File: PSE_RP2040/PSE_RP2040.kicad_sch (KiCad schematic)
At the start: 57 parts, among them IC1 AT25SF128A-SHB-T, IC2 SAM-M8Q-0, J1 USB_B, J2 USB_B_Micro, J3 Conn_01x02, U1 RP2040

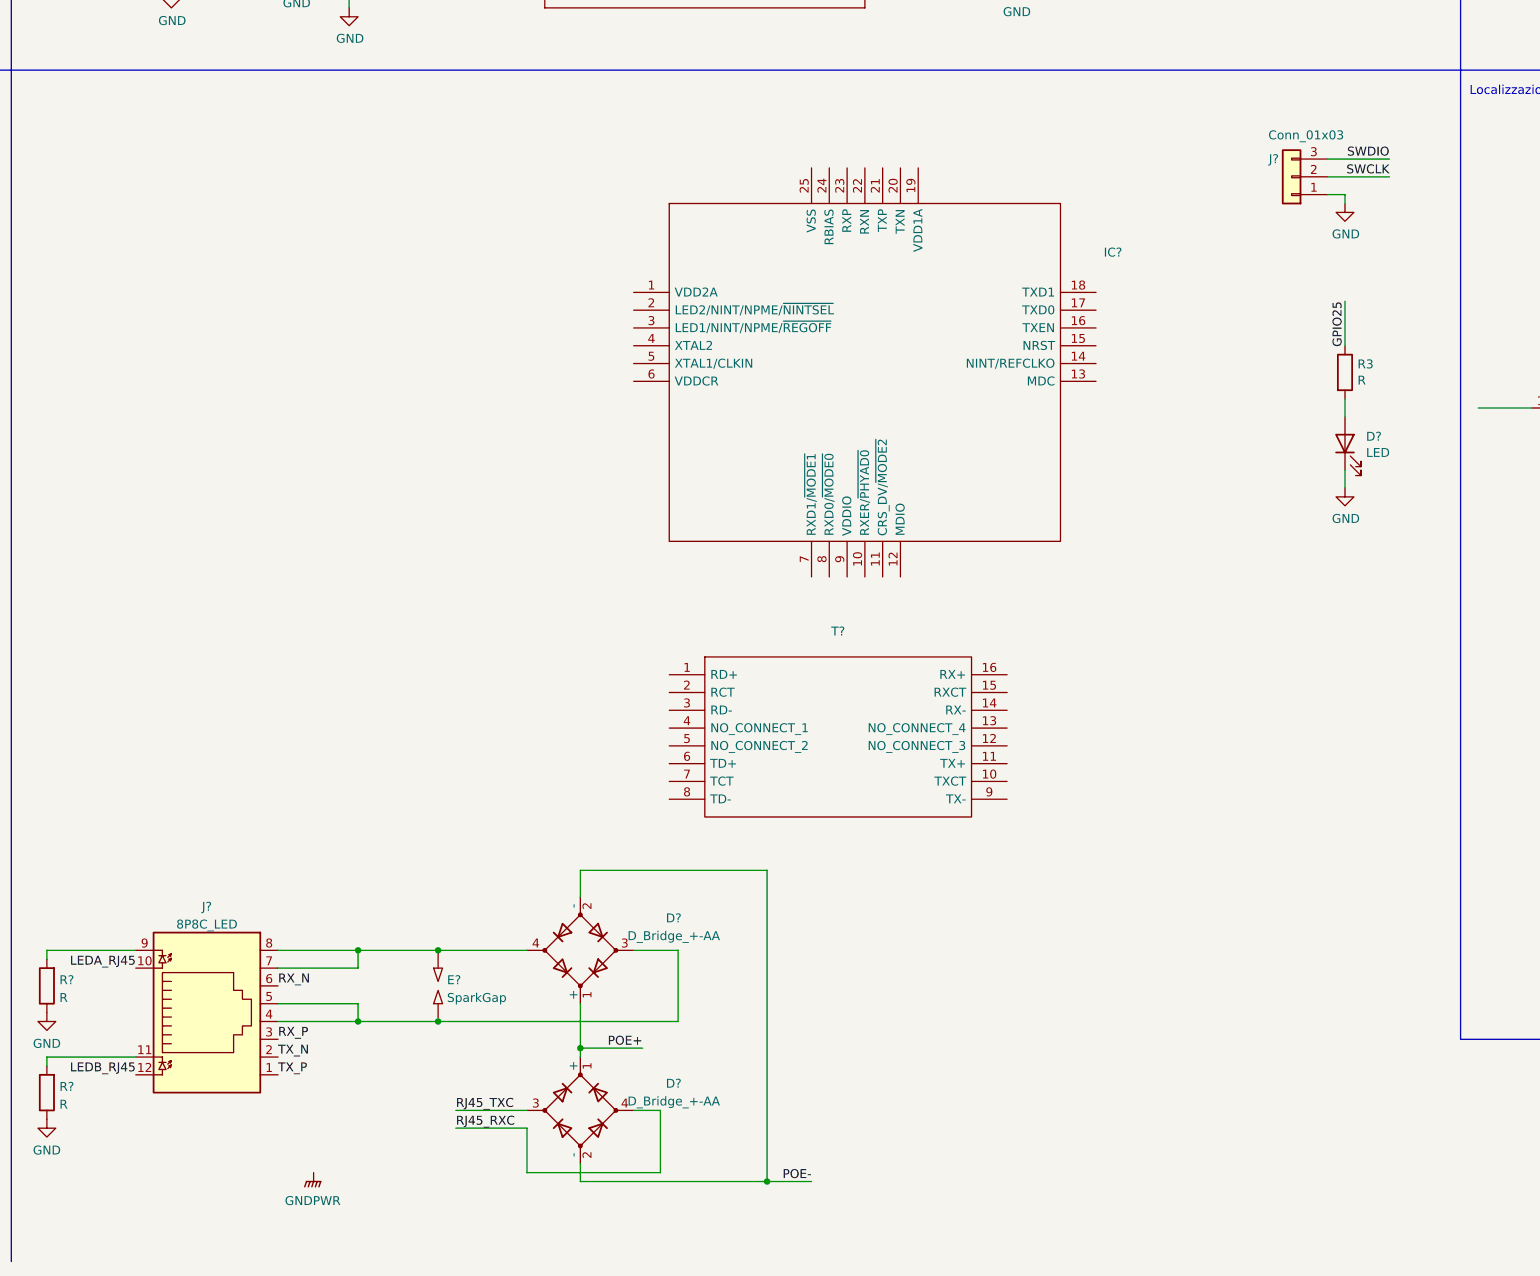
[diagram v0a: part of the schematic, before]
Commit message: sostituzione componenti
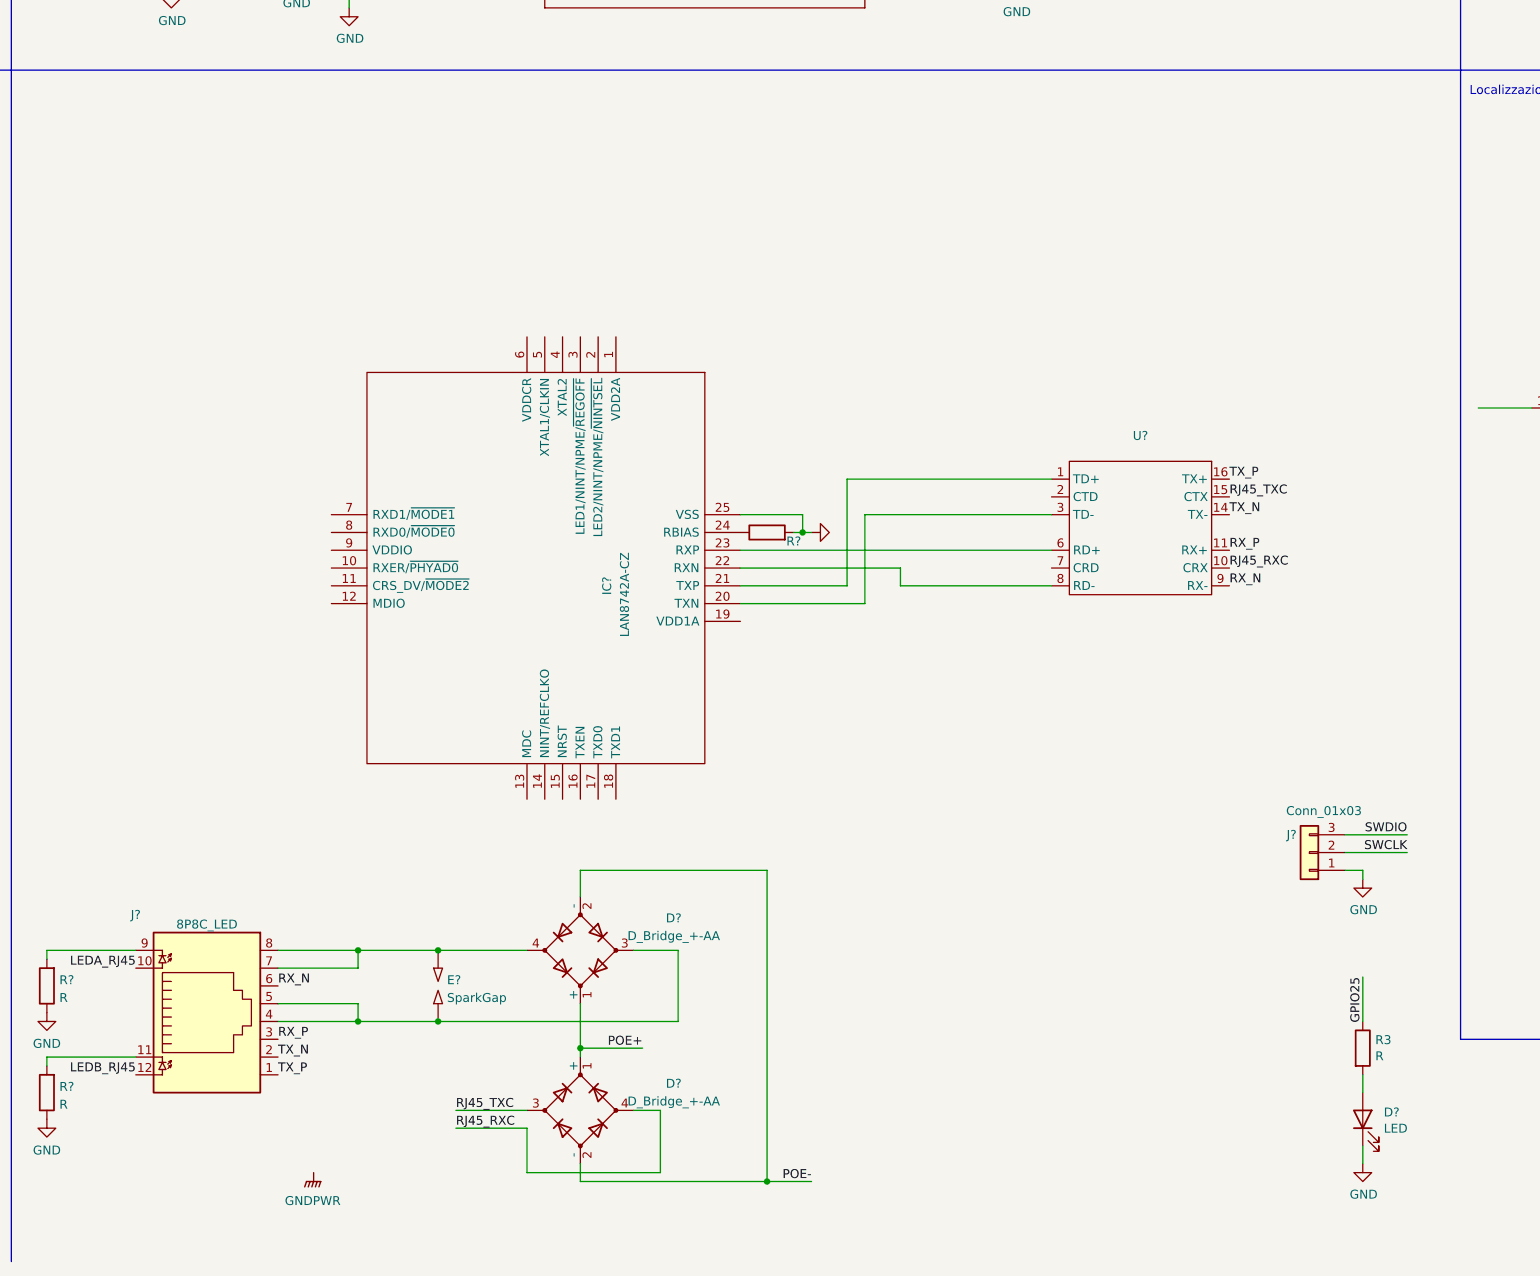
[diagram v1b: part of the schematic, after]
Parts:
- removed T?: (no value), symbol ethernet:749013011
- added R?: (no value), symbol Device:R
- added U?: (no value), symbol ethernet_lib:WE-749013011
- IC?: value (none) -> LAN8742A-CZ; footprint (none) -> QFN50P400X400X100-25N-D
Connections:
- net GND: now also IC?.25 (VSS), R?.2
- net RJ45_RXC: now also U?.10 (CRX)
- net RJ45_TXC: now also U?.15 (CTX)
- net RX_N: now also U?.9 (RX-)
- net RX_P: now also U?.11 (RX+)
- net TX_N: now also U?.14 (TX-)
- net TX_P: now also U?.16 (TX+)
- net at IC?.20 (TXN): now also U?.3 (TD-)
- net at IC?.21 (TXP): now also U?.1 (TD+)
- net at IC?.22 (RXN): now also U?.8 (RD-)
- net at IC?.23 (RXP): now also U?.6 (RD+)
- net at IC?.24 (RBIAS): now also R?.1
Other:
- moved on the sheet: D?, IC?, J?, R3

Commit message: pt.2
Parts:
- added R? (x2): (no value), symbol Device:R
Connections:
- net at IC?.20 (TXN), U?.3 (TD-): now also R?.2
- net at IC?.21 (TXP), U?.1 (TD+): now also R?.2
- net at U?.2 (CTD): now also U?.7 (CRD), R?.1, R?.1
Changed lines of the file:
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@@
   (junction (at 54.61 31.75) (diameter 0) (color 0 0 0 0)
   )
+  (junction (at 227.33 177.8) (diameter 0) (color 0 0 0 0)
+  )
   (junction (at 113.03 95.25) (diameter 0) (color 0 0 0 0)
   )
@@
   (junction (at 34.29 181.61) (diameter 0) (color 0 0 0 0)
   )
+  (junction (at 233.68 172.72) (diameter 0) (color 0 0 0 0)
+  )
   (junction (at 260.35 45.72) (diameter 0) (color 0 0 0 0)
   )
@@
   (junction (at 43.18 240.03) (diameter 0) (color 0 0 0 0)
   )
+  (junction (at 236.22 175.26) (diameter 0) (color 0 0 0 0)
+  )
   (junction (at 341.63 166.37) (diameter 0) (color 0 0 0 0)
   )
@@
   (junction (at 82.55 222.25) (diameter 0) (color 0 0 0 0)
   )
+  (junction (at 233.68 163.83) (diameter 0) (color 0 0 0 0)
+  )
   (junction (at 246.38 35.56) (diameter 0) (color 0 0 0 0)
   )
@@
     (stroke (width 0) (type default) (color 0 0 0 0))
   )
+  (wire (pts (xy 233.68 172.72) (xy 241.3 172.72))
+    (stroke (width 0) (type default) (color 0 0 0 0))
+  )
   (wire (pts (xy 125.73 80.01) (xy 125.73 90.17))
     (stroke (width 0) (type default) (color 0 0 0 0))
@@
     (stroke (width 0) (type default) (color 0 0 0 0))
   )
+  (wire (pts (xy 236.22 163.83) (xy 236.22 175.26))
+    (stroke (width 0) (type default) (color 0 0 0 0))
+  )
   (wire (pts (xy 156.21 265.43) (xy 166.37 265.43))
     (stroke (width 0) (type default) (color 0 0 0 0))
@@
     (stroke (width 0) (type default) (color 0 0 0 0))
   )
-  (wire (pts (xy 212.09 172.72) (xy 241.3 172.72))
+  (wire (pts (xy 212.09 172.72) (xy 233.68 172.72))
     (stroke (width 0) (type default) (color 0 0 0 0))
   )
@@
     (stroke (width 0) (type default) (color 0 0 0 0))
   )
+  (wire (pts (xy 241.3 185.42) (xy 236.22 185.42))
+    (stroke (width 0) (type default) (color 0 0 0 0))
+  )
   (wire (pts (xy 219.71 187.96) (xy 241.3 187.96))
     (stroke (width 0) (type default) (color 0 0 0 0))
@@
     (stroke (width 0) (type default) (color 0 0 0 0))
   )
+  (wire (pts (xy 233.68 163.83) (xy 236.22 163.83))
+    (stroke (width 0) (type default) (color 0 0 0 0))
+  )
   (wire (pts (xy 344.17 166.37) (xy 341.63 166.37))
     (stroke (width 0) (type default) (color 0 0 0 0))
@@
     (stroke (width 0) (type default) (color 0 0 0 0))
   )
+  (wire (pts (xy 236.22 175.26) (xy 241.3 175.26))
+    (stroke (width 0) (type default) (color 0 0 0 0))
+  )
   (wire (pts (xy 34.29 39.37) (xy 40.64 39.37))
     (stroke (width 0) (type default) (color 0 0 0 0))
@@
     (stroke (width 0) (type default) (color 0 0 0 0))
   )
+  (wire (pts (xy 227.33 177.8) (xy 241.3 177.8))
+    (stroke (width 0) (type default) (color 0 0 0 0))
+  )
   (wire (pts (xy 24.13 85.09) (xy 25.4 85.09))
     (stroke (width 0) (type default) (color 0 0 0 0))
@@
     (stroke (width 0) (type default) (color 0 0 0 0))
   )
-  (wire (pts (xy 214.63 177.8) (xy 241.3 177.8))
+  (wire (pts (xy 214.63 177.8) (xy 227.33 177.8))
     (stroke (width 0) (type default) (color 0 0 0 0))
   )
@@
     (stroke (width 0) (type default) (color 0 0 0 0))
   )
+  (wire (pts (xy 227.33 171.45) (xy 227.33 177.8))
+    (stroke (width 0) (type default) (color 0 0 0 0))
+  )
   (wire (pts (xy 161.29 87.63) (xy 154.94 87.63))
     (stroke (width 0) (type default) (color 0 0 0 0))
@@
     (stroke (width 0) (type default) (color 0 0 0 0))
   )
+  (wire (pts (xy 233.68 171.45) (xy 233.68 172.72))
+    (stroke (width 0) (type default) (color 0 0 0 0))
+  )
   (wire (pts (xy 43.18 232.41) (xy 45.72 232.41))
     (stroke (width 0) (type default) (color 0 0 0 0))
@@
     (stroke (width 0) (type default) (color 0 0 0 0))
   )
+  (wire (pts (xy 227.33 163.83) (xy 233.68 163.83))
+    (stroke (width 0) (type default) (color 0 0 0 0))
+  )
   (wire (pts (xy 24.13 46.99) (xy 24.13 50.8))
     (stroke (width 0) (type default) (color 0 0 0 0))
@@
     (stroke (width 0) (type default) (color 0 0 0 0))
   )
+  (wire (pts (xy 236.22 185.42) (xy 236.22 175.26))
+    (stroke (width 0) (type default) (color 0 0 0 0))
+  )
   (wire (pts (xy 34.29 36.83) (xy 40.64 36.83))
     (stroke (width 0) (type default) (color 0 0 0 0))
@@
     (pin "9")
   )
+  (symbol (lib_id "Device:R") (at 233.68 167.64 0) (unit 1)
+    (in_bom yes) (on_board yes)
+    (property "Reference" "R?" (id 0) (at 236.22 166.37 0)
+      (effects (font (size 1.27 1.27)) (justify left))
+    )
+    (property "Value" "" (id 1) (at 236.22 168.91 0)
+      (effects (font (size 1.27 1.27)) (justify left))
+    )
+    (property "Footprint" "" (id 2) (at 231.902 167.64 90)
+      (effects (font (size 1.27 1.27)) hide)
+    )
+    (property "Datasheet" "~" (id 3) (at 233.68 167.64 0)
+      (effects (font (size 1.27 1.27)) hide)
+    )
+    (pin "1")
+    (pin "2")
+  )
   (symbol (lib_id "Connector:8P8C_LED") (at 120.65 250.19 0) (unit 1)
     (in_bom yes) (on_board yes)
@@
     (pin "9")
   )
+  (symbol (lib_id "Device:R") (at 227.33 167.64 0) (unit 1)
+    (in_bom yes) (on_board yes)
+    (property "Reference" "R?" (id 0) (at 220.98 166.37 0)
+      (effects (font (size 1.27 1.27)) (justify left))
+    )
+    (property "Value" "" (id 1) (at 220.98 168.91 0)
+      (effects (font (size 1.27 1.27)) (justify left))
+    )
+    (property "Footprint" "" (id 2) (at 225.552 167.64 90)
+      (effects (font (size 1.27 1.27)) hide)
+    )
+    (property "Datasheet" "~" (id 3) (at 227.33 167.64 0)
+      (effects (font (size 1.27 1.27)) hide)
+    )
+    (pin "1")
+    (pin "2")
+  )
   (symbol (lib_id "ethernet_lib:WE-749013011") (at 254 177.8 0) (unit 1)
     (in_bom yes) (on_board yes) (fields_autoplaced)
@@
       (reference "R?") (unit 1) (value "R") (footprint "")
     )
+    (path "/b9084715-0a94-418f-ae76-9352ce1c66df"
+      (reference "R?") (unit 1) (value "49,9") (footprint "")
+    )
+    (path "/d16bddef-f756-4c62-bafe-b7696d4d053a"
+      (reference "R?") (unit 1) (value "49,9") (footprint "")
+    )
     (path "/e53008a8-734a-4886-bae0-a32174438b79"

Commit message: finito circuito lan
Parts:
- added C?: C, symbol Device:C
- added C? (x5): 100n, symbol Device:C
- added C? (x4): (no value), symbol Device:C
- added C?: (no value), symbol Device:C_Polarized
- added L?: (no value), symbol Device:L
- added R? (x2): 49,9, symbol Device:R
- added R? (x5): 10k, symbol Device:R
- added R? (x4): (no value), symbol Device:R
- added R? (x2): R, symbol Device:R
- added U?: (no value), symbol Power_Protection:USBLC6-4SC6
- added Y?: (no value), symbol Device:Crystal_GND24
- R?: value (none) -> 12k1
- R? (x2): value (none) -> 49,9
- U?: value (none) -> WE-749013011
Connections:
- net +3V3: now also IC?.9 (VDDIO), C?.1, L?.1, R?.2, R?.2, R?.2, R?.2, R?.2
- net GND: now also C?.2, C?.2, C?.2, C?.2, C?.2, C?.2, C?.2, C?.2, C?.2, C?.2, C?.2, R?.2, R?.2, R?.2, U?.2 (GND), Y?.2, Y?.4
- net LEDA_RJ45: now also IC?.3 (LED1/NINT/NPME/~{REGOFF}), R?.1
- net LEDB_RJ45: now also IC?.2 (LED2/NINT/NPME/~{NINTSEL}), R?.1
- net VDD1A: now reaches IC?.1 (VDD2A)
- net VDD1A: now also IC?.19 (VDD1A), R?.1, R?.1, U?.2 (CTD), U?.7 (CRD), C?.1, C?.1, C?.1, C?.1, C?.1, C?.1, L?.2, R?.2, R?.2, U?.5 (VBUS)
- net at IC?.10 (RXER/~{PHYAD0}): now also R?.1
- net CRS: now reaches IC?.11 (CRS_DV/~{MODE2})
- net CRS: now also R?.1
- net MDIO: now reaches IC?.12 (MDIO)
- net MDIO: now also R?.1
- net MDC: now reaches IC?.13 (MDC)
- net at IC?.14 (NINT/REFCLKO): now also R?.1, R?.2
- net NRST: now reaches IC?.15 (NRST)
- net TXEN: now reaches IC?.16 (TXEN)
- net TXD0: now reaches IC?.17 (TXD0)
- net TXD1: now reaches IC?.18 (TXD1)
- net at IC?.20 (TXN), R?.2, U?.3 (TD-): now also U?.4 (I/O3)
- net at IC?.21 (TXP), R?.2, U?.1 (TD+): now also U?.3 (I/O2)
- net at IC?.22 (RXN), U?.8 (RD-): now also R?.1, U?.6 (I/O4)
- net at IC?.23 (RXP), U?.6 (RD+): now also R?.1, U?.1 (I/O1)
- net at IC?.4 (XTAL2): now also C?.1, Y?.3
- net at IC?.5 (XTAL1/CLKIN): now also C?.1, Y?.1
- net at IC?.6 (VDDCR): now also C?.1, C?.1
- net at IC?.7 (RXD1/~{MODE1}): now also R?.1, R?.2
- net at IC?.8 (RXD0/~{MODE0}): now also R?.1, R?.2
- new net NINT: R?.1
- new net RXD1: R?.1
- new net RXDO: R?.1
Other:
- moved on the sheet: R?, U?

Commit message: schematico completato
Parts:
- C?: value (none) -> 470p
- C?: value (none) -> 1u
- C?: value (none) -> 10u 16V
- C?: value (none) -> 100n
- C?: value (none) -> C
- L?: value (none) -> L
- R?: value (none) -> R
- R? (x3): value (none) -> 10k
- U?: value (none) -> USBLC6-4SC6; footprint (none) -> Package_TO_SOT_SMD:SOT-23-6
- Y?: value (none) -> Crystal_GND24
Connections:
- net POE+ renamed poe+
- net POE- renamed poe-
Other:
- added sheet poe (untitled.kicad_sch)

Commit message: rtc aggiunta
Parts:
- removed C1, C2: 47u, symbol Device:C
- removed C?: 1u, symbol Device:C
- removed C?: 100n, symbol Device:C
- removed D? (x2): MBR1020VL, Diode_SMD:D_SOD-123F, symbol Diode:MBR1020VL
- removed L2: 2U2, symbol Device:L
- removed R2, R8: 100k, symbol Device:R
- removed U?: MCP1703A-3302_SOT23, Package_TO_SOT_SMD:SOT-23, symbol Regulator_Linear:MCP1703A-3302_SOT23
- removed U?: RT6150A_B, symbol PSE_RP2040-rescue:RT6150A_B-buck_converter
- added U?: (no value), symbol Timer_RTC:PCF8563T

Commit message: Presentazione
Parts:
- U?: value (none) -> PCF8563T; footprint (none) -> Package_SO:SOIC-8_3.9x4.9mm_P1.27mm
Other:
- sheet poe renamed Alimentazioni
- note added: "RTC"
- note removed: "Alimentazione"
- moved on the sheet: U?
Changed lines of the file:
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@@
     (effects (font (size 1.27 1.27)) (justify left bottom))
   )
-  (text "Alimentazione\n" (at 19.05 132.08 0)
+  (text "RTC" (at 19.05 132.08 0)
     (effects (font (size 1.27 1.27)) (justify left bottom))
   )
@@
     (pin "2")
   )
-  (symbol (lib_id "Timer_RTC:PCF8563T") (at 67.31 132.08 0) (unit 1)
-    (in_bom yes) (on_board yes) (fields_autoplaced)
-    (property "Reference" "U?" (id 0) (at 69.3294 120.7602 0)
-      (effects (font (size 1.27 1.27)) (justify left))
-    )
-    (property "Value" "" (id 1) (at 69.3294 123.2971 0)
-      (effects (font (size 1.27 1.27)) (justify left))
-    )
-    (property "Footprint" "" (id 2) (at 67.31 132.08 0)
-      (effects (font (size 1.27 1.27)) hide)
-    )
-    (property "Datasheet" "https://assets.nexperia.com/documents/data-sheet/PCF8563.pdf" (id 3) (at 67.31 132.08 0)
+  (symbol (lib_id "Timer_RTC:PCF8563T") (at 50.8 149.86 0) (unit 1)
+    (in_bom yes) (on_board yes) (fields_autoplaced)
+    (property "Reference" "U?" (id 0) (at 52.8194 138.5402 0)
+      (effects (font (size 1.27 1.27)) (justify left))
+    )
+    (property "Value" "PCF8563T" (id 1) (at 52.8194 141.0771 0)
+      (effects (font (size 1.27 1.27)) (justify left))
+    )
+    (property "Footprint" "Package_SO:SOIC-8_3.9x4.9mm_P1.27mm" (id 2) (at 50.8 149.86 0)
+      (effects (font (size 1.27 1.27)) hide)
+    )
+    (property "Datasheet" "https://assets.nexperia.com/documents/data-sheet/PCF8563.pdf" (id 3) (at 50.8 149.86 0)
       (effects (font (size 1.27 1.27)) hide)
     )
@@
     (stroke (width 0.1524) (type solid) (color 0 0 0 0))
     (fill (color 0 0 0 0.0000))
-    (property "Sheet name" "poe" (id 0) (at 215.9 241.8584 0)
+    (property "Sheet name" "Alimentazioni" (id 0) (at 215.9 241.8584 0)
       (effects (font (size 1.27 1.27)) (justify left bottom))
     )
